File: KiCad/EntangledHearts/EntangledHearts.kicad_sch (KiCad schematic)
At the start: 8 parts

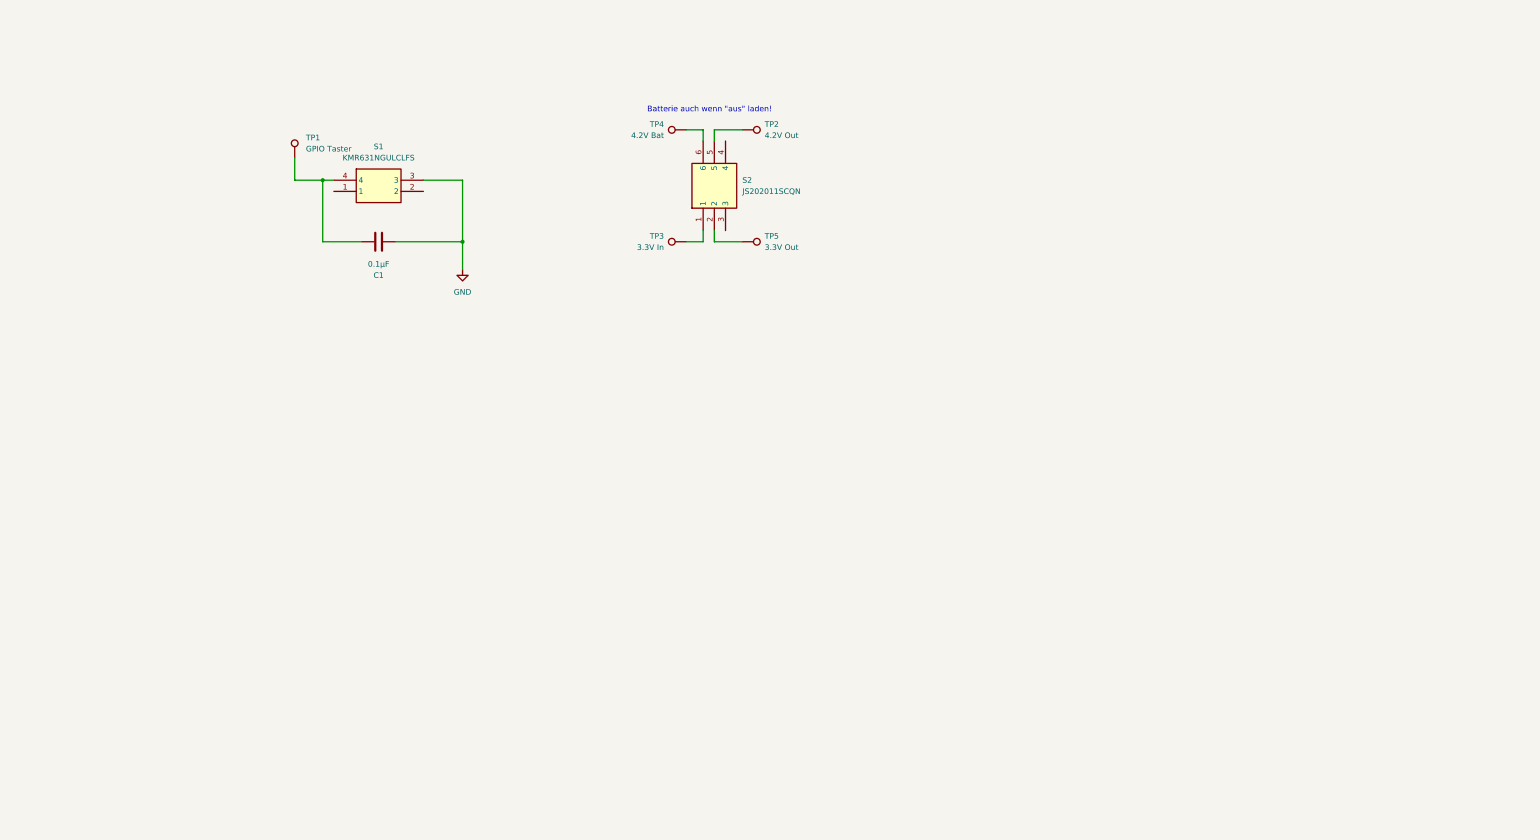
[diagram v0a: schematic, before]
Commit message: ADD: schematics for main circuits added
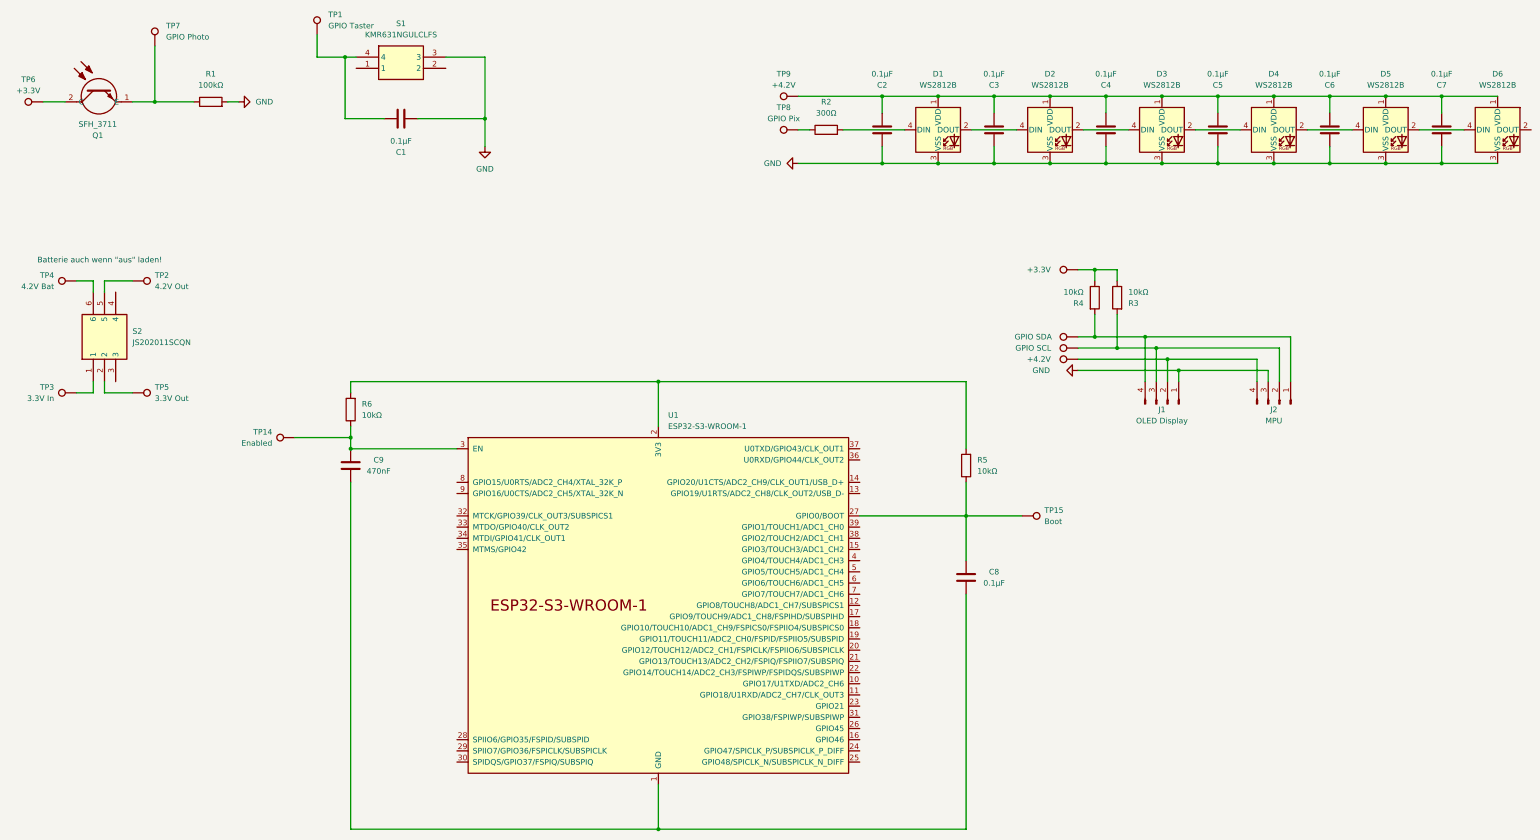
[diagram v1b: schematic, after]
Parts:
- added C2, C3, C4, C5, C6, C7, C8: 0.1µF, Capacitor_SMD:C_0805_2012Metric, symbol Device:C
- added C9: 470nF, Capacitor_SMD:C_0805_2012Metric, symbol Device:C
- added D1, D2, D3, D4, D5, D6: WS2812B, LED_SMD:LED_WS2812B_PLCC4_5.0x5.0mm_P3.2mm, symbol LED:WS2812B
- added J1: OLED Display, symbol Connector:Conn_01x04_Pin
- added J2: MPU, symbol Connector:Conn_01x04_Pin
- added Q1: SFH_3711, SFH3711, symbol SFH_3711:SFH_3711
- added R1: 100kΩ, symbol Device:R
- added R2: 300Ω, symbol Device:R
- added R3, R4, R5, R6: 10kΩ, symbol Device:R
- added TP10, TP9: +4.2V, symbol Connector:TestPoint
- added TP11: GPIO SCL, symbol Connector:TestPoint
- added TP12: GPIO SDA, symbol Connector:TestPoint
- added TP13, TP6: +3.3V, symbol Connector:TestPoint
- added TP14: Enabled, symbol Connector:TestPoint
- added TP15: Boot, symbol Connector:TestPoint
- added TP7: GPIO Photo, symbol Connector:TestPoint
- added TP8: GPIO Pix, symbol Connector:TestPoint
- added U1: ESP32-S3-WROOM-1, PCM_Espressif:ESP32-S3-WROOM-1, symbol PCM_Espressif:ESP32-S3-WROOM-1
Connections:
- net GND: now also C2.2, C3.2, C4.2, C5.2, C6.2, C7.2, D1.3 (VSS), D2.3 (VSS), D3.3 (VSS), D4.3 (VSS), D5.3 (VSS), D6.3 (VSS), J1.1 (Pin_1), J2.3 (Pin_3), R1.2
- new net: Q1.1 (E), R1.1, TP7.1
- new net: J1.3 (Pin_3), J2.2 (Pin_2), R3.2, TP11.1
- new net: C9.2, R6.1, TP14.1, U1.3 (EN)
- new net: J1.2 (Pin_2), J2.4 (Pin_4), TP10.1
- new net: J1.4 (Pin_4), J2.1 (Pin_1), R4.2, TP12.1
- new net: C8.2, R5.1, TP15.1, U1.27 (GPIO0/BOOT)
- new net: R2.1, TP8.1
- new net: R3.1, R4.1, TP13.1
- new net: C2.1, C3.1, C4.1, C5.1, C6.1, C7.1, D1.1 (VDD), D2.1 (VDD), D3.1 (VDD), D4.1 (VDD), D5.1 (VDD), D6.1 (VDD), TP9.1
- new net: D5.2 (DOUT), D6.4 (DIN)
- new net: D2.2 (DOUT), D3.4 (DIN)
- new net: D1.2 (DOUT), D2.4 (DIN)
- new net: C8.1, C9.1, U1.1 (GND), U1.40 (GND), U1.41 (GND)
- new net: R5.2, R6.2, U1.2 (3V3)
- new net: Q1.2 (C), TP6.1
- new net: D1.4 (DIN), R2.2
- new net: D4.2 (DOUT), D5.4 (DIN)
- new net: D3.2 (DOUT), D4.4 (DIN)
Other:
- moved on the sheet: C1, S1, S2, TP1, TP2, TP3, TP4, TP5

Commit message: ADD: all parts added
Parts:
- removed TP10, TP9: +4.2V, symbol Connector:TestPoint
- removed TP13, TP6: +3.3V, symbol Connector:TestPoint
- removed TP5: 3.3V Out, symbol Connector:TestPoint
- added C10, C11: 4.7µF, symbol Device:C
- added C12, C14, C15: 1µF, symbol Device:C
- added C13: 470pF, symbol Device:C
- added D7: LED, symbol Device:LED
- added J3: USB4135-GF-A, USB4135GFA, symbol USB4135-GF-A:USB4135-GF-A
- added R7: 2kΩ, symbol Device:R
- added R8: 330Ω, symbol Device:R
- added TP16: + Bat, symbol Connector:TestPoint
- added U2: MCP73831-2-OT, Package_TO_SOT_SMD:SOT-23-5, symbol Battery_Management:MCP73831-2-OT
- added U3: TC1185-xCT, Package_TO_SOT_SMD:SOT-23-5, symbol Regulator_Linear:TC1185-xCT
- TP11: value GPIO SCL -> SCL
- TP12: value GPIO SDA -> SDA
- TP2: value 4.2V Out -> Boot
- TP3: value 3.3V In -> Boot
- TP4: value 4.2V Bat -> - Bat
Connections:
- net GND is gone; now on an unnamed net: C1.2, C2.2, C3.2, C4.2, C5.2, C6.2, C7.2, D1.3 (VSS), D2.3 (VSS), D3.3 (VSS), D4.3 (VSS), D5.3 (VSS), D6.3 (VSS), J1.1 (Pin_1), J2.3 (Pin_3), R1.2, S1.3
- net at TP2.1: now also U1.37 (U0TXD/GPIO43/CLK_OUT1); no longer S2.5
- net at J1.3 (Pin_3), J2.2 (Pin_2), TP11.1: now also R4.1; no longer R3.2
- net at J1.2 (Pin_2), J2.4 (Pin_4): now also C2.1, C3.1, C4.1, C5.1, C6.1, C7.1, D1.1 (VDD), D2.1 (VDD), D3.1 (VDD), D4.1 (VDD), D5.1 (VDD), D6.1 (VDD), S2.2, C14.1, U3.1 (VIN), U3.3 (~{SHDN})
- net at J1.4 (Pin_4), J2.1 (Pin_1), TP12.1: now also R3.1; no longer R4.2
- net at C8.1, C9.1, U1.1 (GND)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: now also TP4.1, C10.2, C11.2, C12.2, C13.2, C14.2, C15.2, J3.A12, J3.B12, J3.MP1, J3.MP2, J3.MP3, J3.MP4, R7.2, U2.2 (V_{SS}), U3.2 (GND)
- net at R5.2, R6.2, U1.2 (3V3): now also Q1.2 (C), R3.2, R4.2, C15.1, U3.5 (VOUT)
- net at U1.36 (U0RXD/GPIO44/CLK_OUT2): now also TP3.1
- net at S2.6: no longer TP4.1
- net at S2.1: now also C11.1, C12.1, TP16.1, U2.3 (V_{BAT}); no longer TP3.1
- new net: C10.1, J3.A9, J3.B9, R8.1, U2.4 (V_{DD})
- new net: C13.1, U3.4 (Bypass)
- new net: D7.1 (K), U2.1 (STAT)
- new net: D7.2 (A), R8.2
- new net: R7.1, U2.5 (PROG)
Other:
- note removed: "Batterie auch wenn "aus" laden!"
- moved on the sheet: C1, C2, C3, C4, C5, C6, C7, C8, C9, D1, D2, D3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

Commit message: ADD: final touches for first plot
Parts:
- removed TP1: GPIO Taster, symbol Connector:TestPoint
- removed TP11: SCL, symbol Connector:TestPoint
- removed TP12: SDA, symbol Connector:TestPoint
- removed TP14: Enabled, symbol Connector:TestPoint
- removed TP15, TP2, TP3: Boot, symbol Connector:TestPoint
- removed TP7: GPIO Photo, symbol Connector:TestPoint
- removed TP8: GPIO Pix, symbol Connector:TestPoint
- added S_BOOT: Boot, symbol Connector:TestPoint
- added S_EN: Enabled, symbol Connector:TestPoint
- added S_RXD: RXD (twist), symbol Connector:TestPoint
- added S_TXD: TXD (twist), symbol Connector:TestPoint
- added TPS_GND: GND, symbol Connector:TestPoint
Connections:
- net at U1.36 (U0RXD/GPIO44/CLK_OUT2): now also S_RXD.1
- net at C1.1, S1.4: now also U1.39 (GPIO1/TOUCH1/ADC1_CH0)
- net at C1.2, C10.2, C11.2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: now also TPS_GND.1
- net at Q1.1 (E), R1.1: now also U1.38 (GPIO2/TOUCH2/ADC1_CH1)
- net at J1.3 (Pin_3), J2.2 (Pin_2), R4.1: now also U1.20 (GPIO12/TOUCH12/ADC2_CH1/FSPICLK/FSPIIO6/SUBSPICLK)
- net at C9.2, R6.1, U1.3 (EN): now also S_EN.1
- net at J1.4 (Pin_4), J2.1 (Pin_1), R3.1: now also U1.19 (GPIO11/TOUCH11/ADC2_CH0/FSPID/FSPIIO5/SUBSPID)
- net at C8.2, R5.1, U1.27 (GPIO0/BOOT): now also S_BOOT.1
- net at R2.1: now also U1.23 (GPIO21)
- net at U1.37 (U0TXD/GPIO43/CLK_OUT1): now also S_TXD.1
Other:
- note added: "Internal PullUp"
- moved on the sheet: C1, C2, C3, C4, C5, C6, C7, C8, C9, D1, D2, D3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

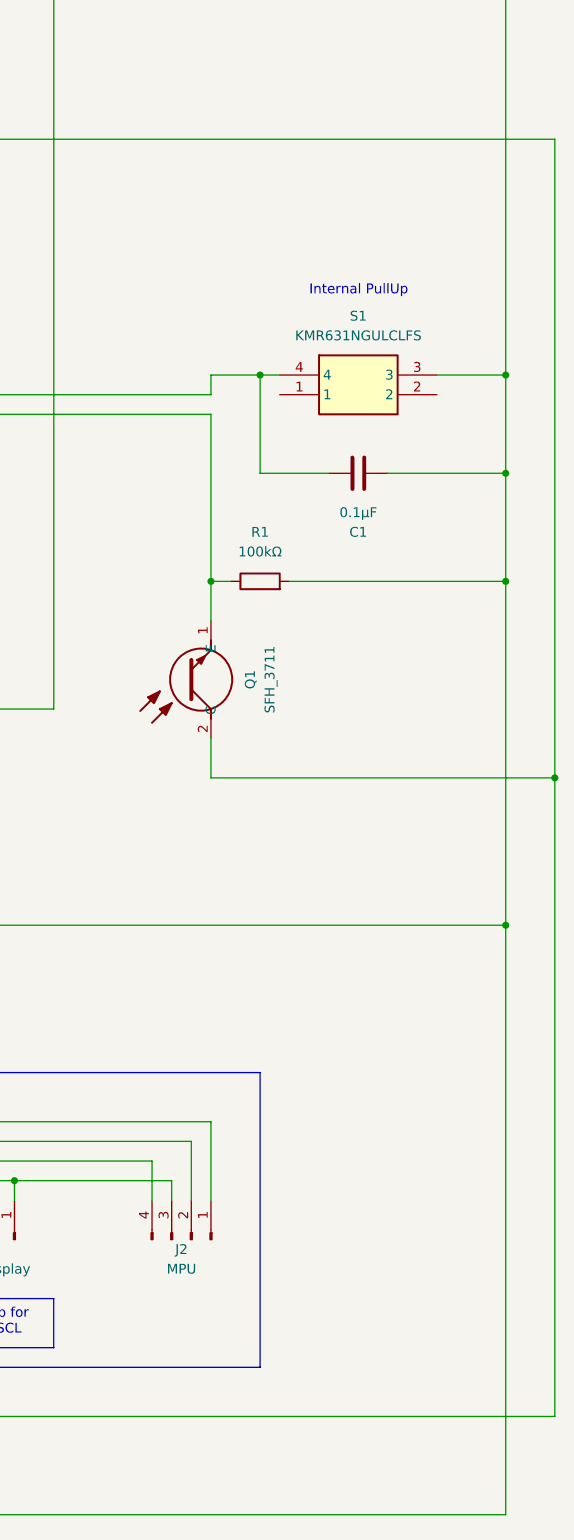
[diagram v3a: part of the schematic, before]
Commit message: CHG: GPIO photo low-active
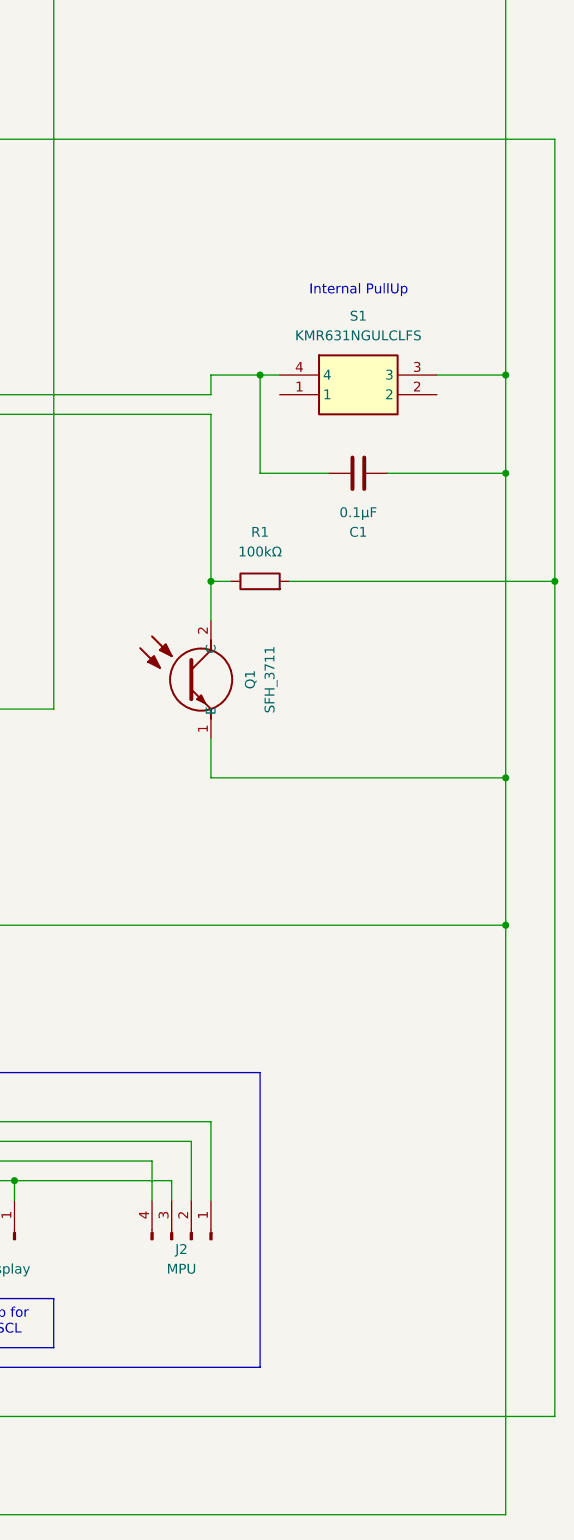
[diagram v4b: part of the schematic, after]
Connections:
- net at C1.2, C10.2, C11.2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: now also Q1.1 (E); no longer R1.2
- net at R1.1, U1.38 (GPIO2/TOUCH2/ADC1_CH1): now also Q1.2 (C); no longer Q1.1 (E)
- net at C15.1, R3.2, R4.2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: now also R1.2; no longer Q1.2 (C)

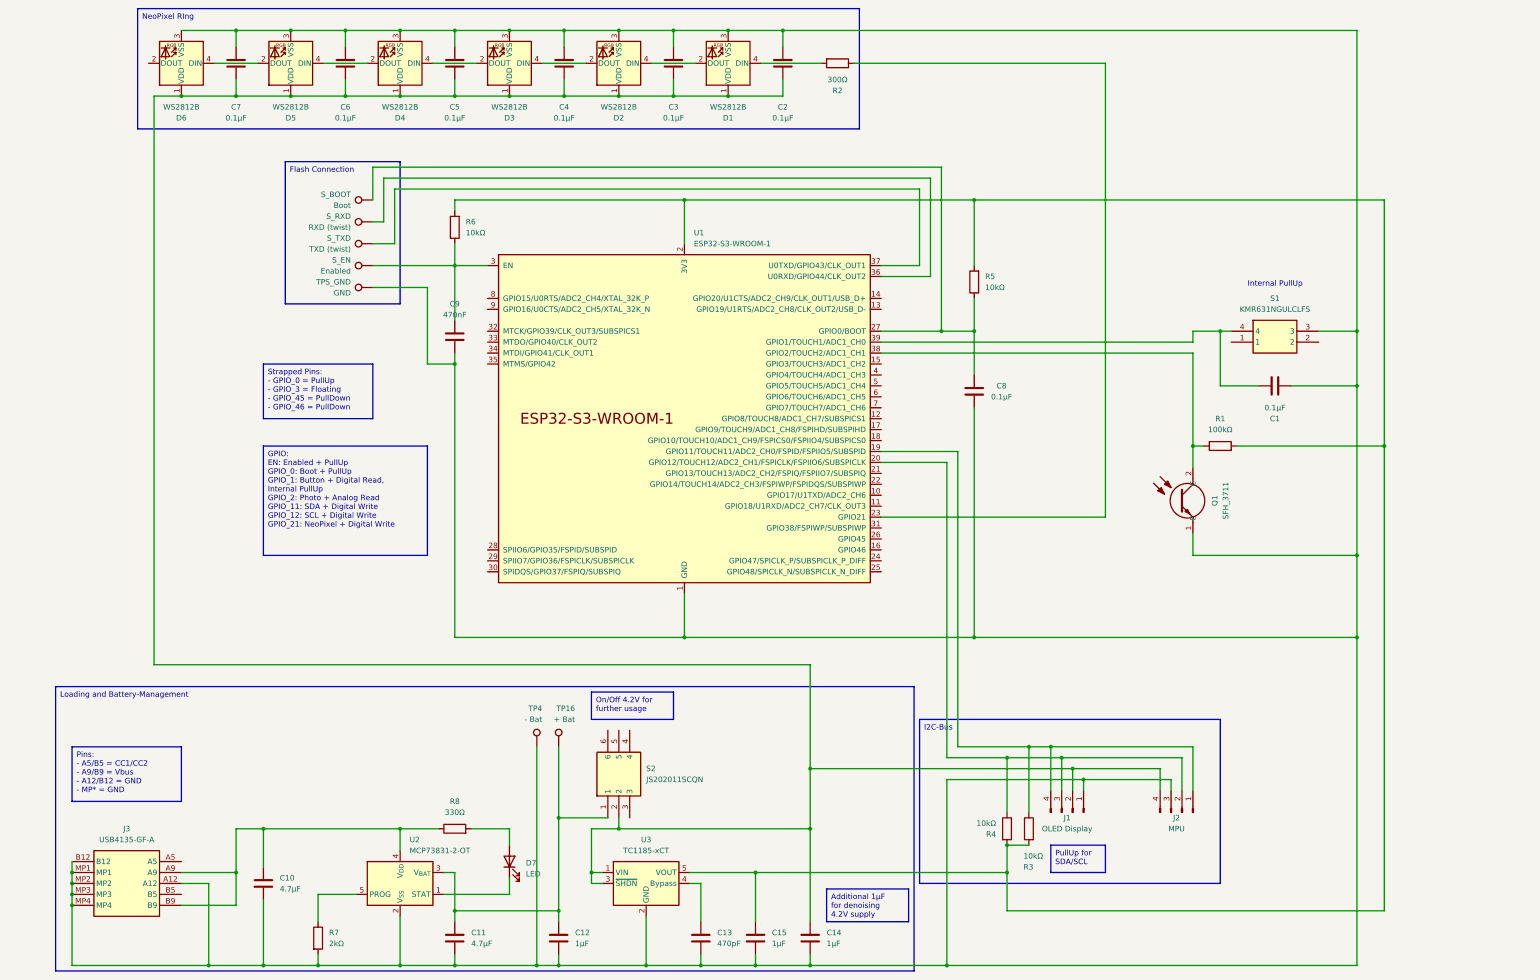
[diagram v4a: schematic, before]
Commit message: ADD: flashing circuit added
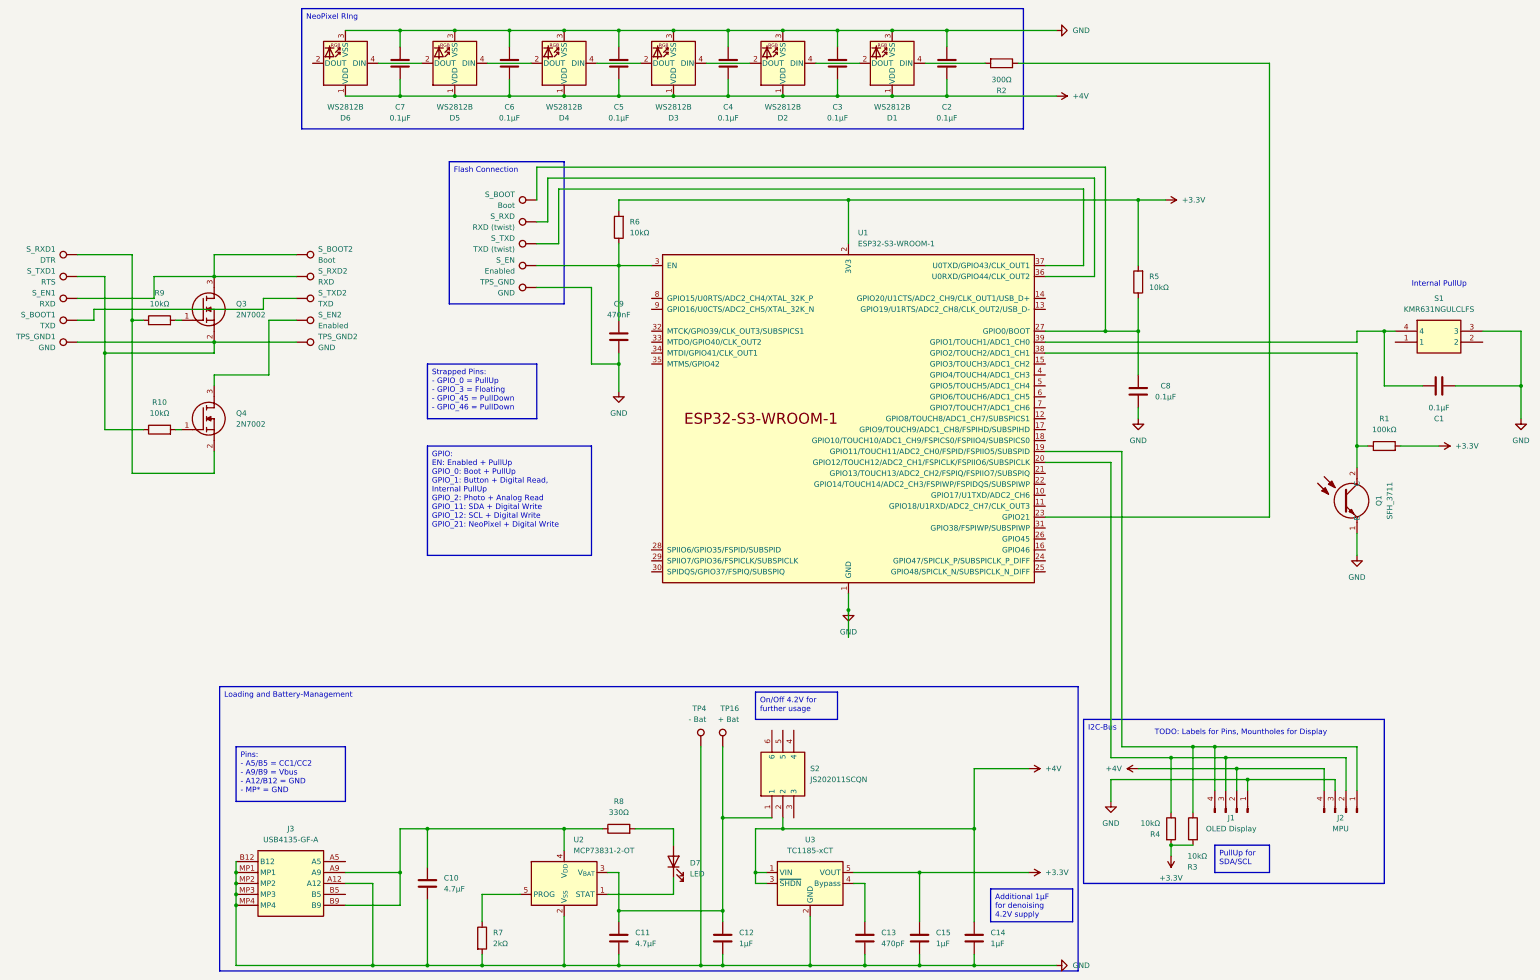
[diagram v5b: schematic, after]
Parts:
- added Q3, Q4: 2N7002, SOT96P240X120-3N, symbol 2N7002:2N7002
- added R10, R9: 10kΩ, Resistor_SMD:R_0805_2012Metric, symbol Device:R
- added S_BOOT1, S_TXD2: TXD, symbol Connector:TestPoint
- added S_BOOT2: Boot, symbol Connector:TestPoint
- added S_EN1, S_RXD2: RXD, symbol Connector:TestPoint
- added S_EN2: Enabled, symbol Connector:TestPoint
- added S_RXD1: DTR, symbol Connector:TestPoint
- added S_TXD1: RTS, symbol Connector:TestPoint
- added TPS_GND1, TPS_GND2: GND, symbol Connector:TestPoint
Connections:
- net GND: now reaches C1.2, C10.2, C11.2, C12.2, C13.2, C14.2, C15.2, C2.2, C3.2, C4.2, C5.2, C6.2, C7.2, C8.1, C9.1, D1.3 (VSS), D2.3 (VSS), D3.3 (VSS), D4.3 (VSS), D5.3 (VSS), D6.3 (VSS), J1.1 (Pin_1), J2.3 (Pin_3), J3.A12, J3.B12, J3.MP1, J3.MP2, J3.MP3, J3.MP4, Q1.1 (E), R7.2, S1.3, TP4.1, TPS_GND.1, U1.1 (GND), U1.40 (GND), U1.41 (GND), U2.2 (V_{SS}), U3.2 (GND)
- net +3.3V: now reaches C15.1, R1.2, R3.2, R4.2, R5.2, R6.2, U1.2 (3V3), U3.5 (VOUT)
- net +4V: now reaches C14.1, C2.1, C3.1, C4.1, C5.1, C6.1, C7.1, D1.1 (VDD), D2.1 (VDD), D3.1 (VDD), D4.1 (VDD), D5.1 (VDD), D6.1 (VDD), J1.2 (Pin_2), J2.4 (Pin_4), S2.2, U3.1 (VIN), U3.3 (~{SHDN})
- new net: S_BOOT1.1, S_TXD2.1
- new net: Q4.3 (D), S_EN2.1
- new net: Q3.3 (D), S_BOOT2.1, S_EN1.1, S_RXD2.1
- new net: Q4.2 (S), R9.1, S_RXD1.1
- new net: Q3.2 (S), R10.1, S_TXD1.1, TPS_GND1.1, TPS_GND2.1
- new net: Q3.1 (G), R9.2
- new net: Q4.1 (G), R10.2
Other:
- note added: "TODO: Labels for Pins, Mountholes for Display"
- moved on the sheet: C1, C10, C11, C12, C13, C14, C15, C2, C3, C4, C5, C6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
